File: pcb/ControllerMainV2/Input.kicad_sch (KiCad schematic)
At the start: 10 parts, among them IC21 TMUX6112PWR, U13 TL072

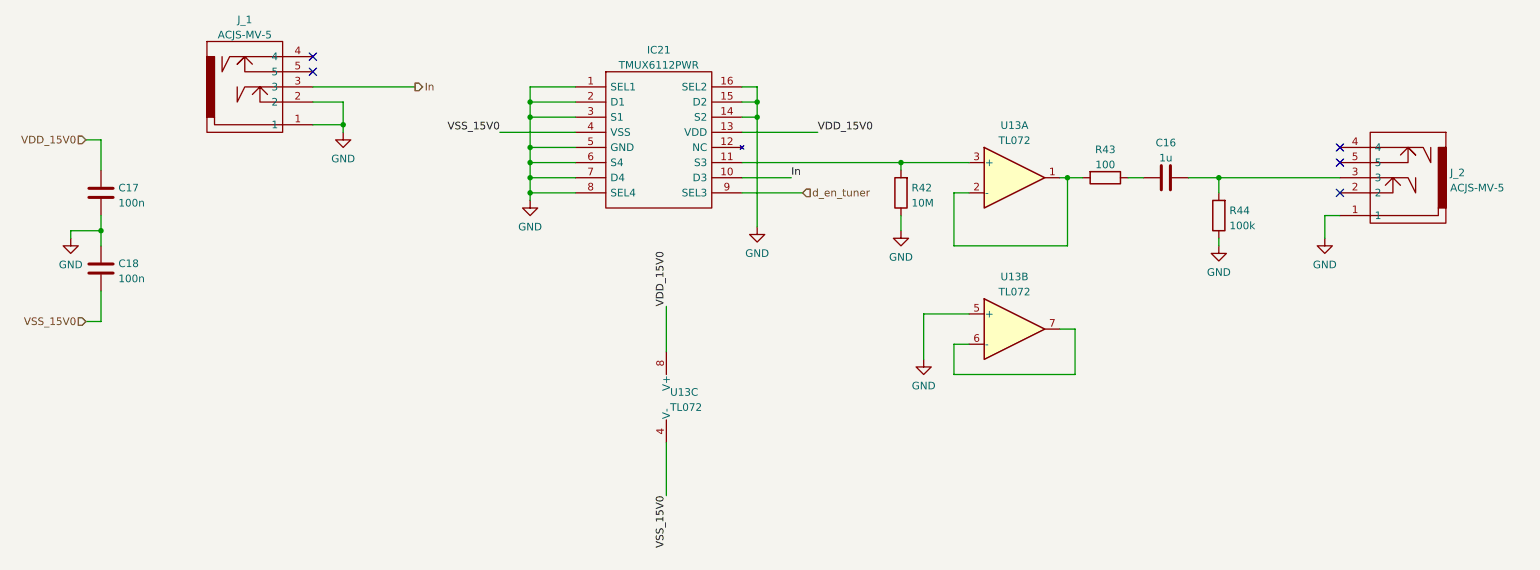
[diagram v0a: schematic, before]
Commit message: New version with smaller enclosure
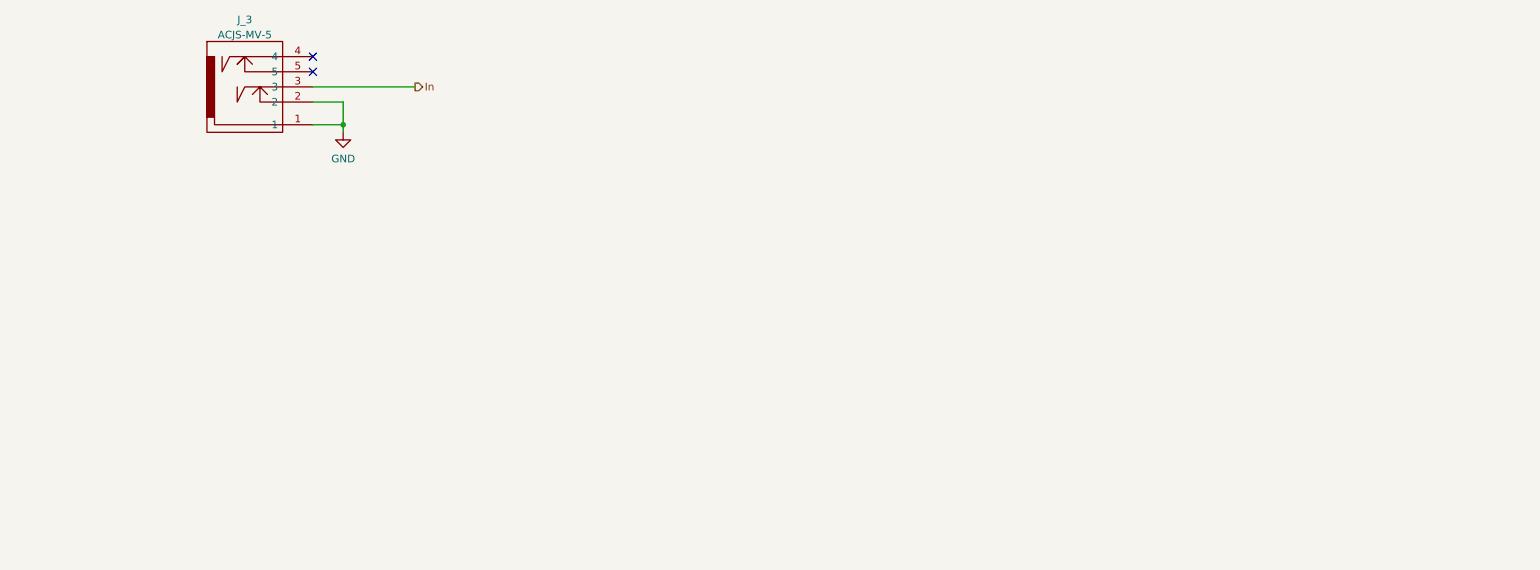
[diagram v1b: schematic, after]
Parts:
- removed C16: 1u, Capacitor_SMD:C_1206_3216Metric_Pad1.33x1.80mm_HandSolder, symbol Device:C
- removed C17, C18: 100n, Capacitor_SMD:C_1206_3216Metric_Pad1.33x1.80mm_HandSolder, symbol Device:C
- removed IC21: TMUX6112PWR, SamacSys_Parts:SOP65P640X120-16N, symbol SamacSys_Parts:TMUX6112PWR
- removed J_2: ACJS-MV-5, SamacSys_Parts:ACJSMV5, symbol Aphenol:ACJS-MV-5
- removed R42: 10M, Resistor_SMD:R_1206_3216Metric_Pad1.30x1.75mm_HandSolder, symbol Device:R
- removed R43: 100, Resistor_SMD:R_1206_3216Metric_Pad1.30x1.75mm_HandSolder, symbol Device:R
- removed R44: 100k, Resistor_SMD:R_1206_3216Metric_Pad1.30x1.75mm_HandSolder, symbol Device:R
- removed U13: TL072, SamacSys_Parts:SOIC127P600X175-8N, symbol Amplifier_Operational:TL072
- renumbered J_1 to J_3
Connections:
- no-connect marks 5 -> 2
